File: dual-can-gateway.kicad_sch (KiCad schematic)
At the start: 82 parts, among them J3 Conn_01x02_Pin, Q1 AO3401A, Q2 2N7002, U1 STM32F446RETx, U2 STM32F446RETx, U3 ESP32-WROOM-32UE, U4 TJA1044GT-3, U5 TJA1044GT-3, U6 TJA1055T, U7 TJA1055T, U8 LM2596S-5, U9 AMS1117-3.3

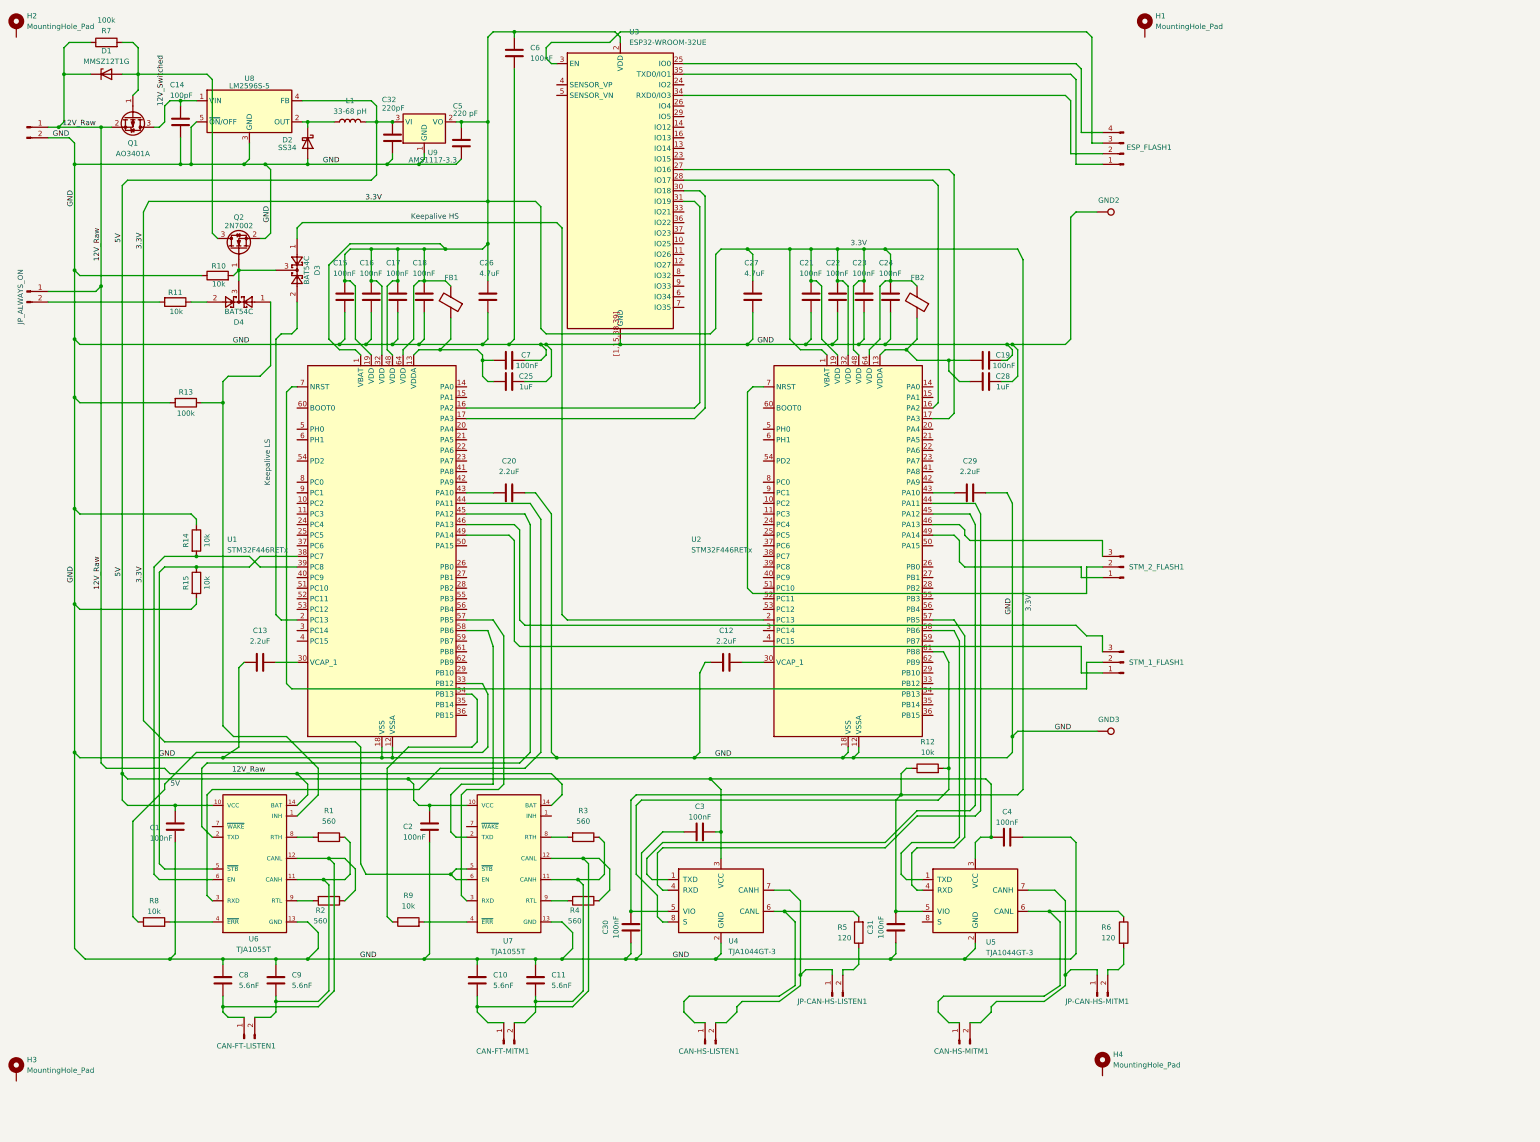
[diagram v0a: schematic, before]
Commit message: proper caps added
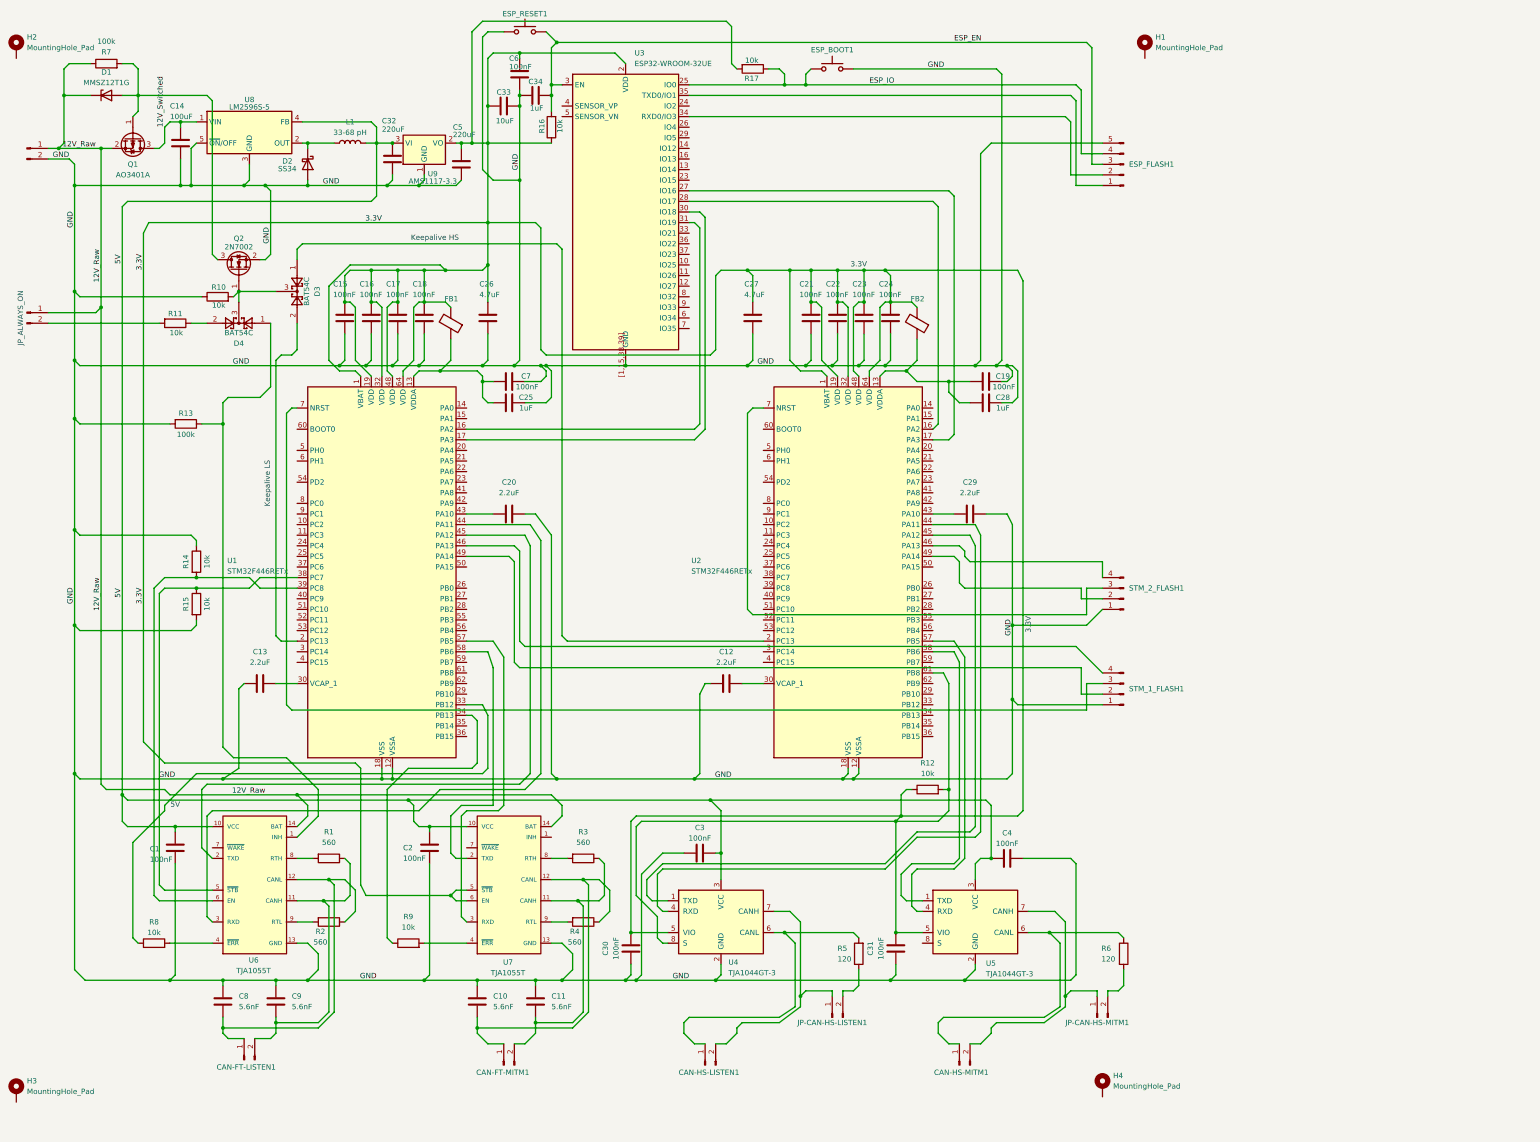
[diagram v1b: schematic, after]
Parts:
- removed ESP_FLASH1: Conn_01x04_Pin, Connector_PinHeader_2.54mm:PinHeader_1x04_P2.54mm_Vertical, symbol Connector:Conn_01x04_Pin
- removed GND2, GND3: TestPoint, Connector_PinHeader_2.54mm:PinHeader_1x01_P2.54mm_Vertical, symbol Connector:TestPoint
- removed STM_1_FLASH1, STM_2_FLASH1: Conn_01x03_Pin, Connector_PinHeader_2.54mm:PinHeader_1x03_P2.54mm_Vertical, symbol Connector:Conn_01x03_Pin
- added C33: 10uF, Capacitor_SMD:C_0805_2012Metric, symbol Device:C
- added C34: 1uF, Capacitor_SMD:C_0805_2012Metric, symbol Device:C
- added ESP_BOOT1: ESP_BOOT, Button_Switch_SMD:SW_Tactile_SPST_NO_Straight_CK_PTS636Sx25SMTRLFS, symbol Switch:SW_Push
- added ESP_FLASH1: Conn_01x05_Pin, Connector_PinHeader_2.54mm:PinHeader_1x05_P2.54mm_Vertical, symbol Connector:Conn_01x05_Pin
- added ESP_RESET1: ESP_RESET, Button_Switch_SMD:SW_Tactile_SPST_NO_Straight_CK_PTS636Sx25SMTRLFS, symbol Switch:SW_Push
- added R16, R17: 10k, Resistor_SMD:R_0805_2012Metric, symbol Device:R
- added STM_1_FLASH1, STM_2_FLASH1: Conn_01x04_Pin, Connector_PinHeader_2.54mm:PinHeader_1x04_P2.54mm_Vertical, symbol Connector:Conn_01x04_Pin
- C14: value 100pF -> 100uF; footprint Capacitor_SMD:C_0805_2012Metric -> Capacitor_Tantalum_SMD:CP_EIA-7343-40_Kemet-Y_HandSolder
- C32: value 220pF -> 220uF; footprint Capacitor_SMD:C_0805_2012Metric -> Capacitor_Tantalum_SMD:CP_EIA-6032-28_Kemet-C_HandSolder
- C5: value 220 pF -> 220uF; footprint Capacitor_SMD:C_0805_2012Metric -> Capacitor_Tantalum_SMD:CP_EIA-6032-28_Kemet-C_HandSolder
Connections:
- net 3.3V: now also R12.2, U2.61 (PB8), U4.8 (S), C33.1, R16.1, R17.2
- net GND: now also C33.2, C34.2, ESP_BOOT1.2, ESP_FLASH1.5 (Pin_5), ESP_RESET1.1, STM_1_FLASH1.1 (Pin_1), STM_2_FLASH1.1 (Pin_1)
- net at U3.35 (TXD0/IO1): now also ESP_FLASH1.1 (Pin_1)
- net at U3.34 (RXD0/IO3): now also ESP_FLASH1.2 (Pin_2)
- net ESP_EN: now reaches U3.3 (EN)
- net ESP_EN: now also C34.1, ESP_FLASH1.3 (Pin_3), ESP_RESET1.2, R16.2
- net ESP_IO: now reaches U3.25 (IO0)
- net ESP_IO: now also ESP_BOOT1.1, ESP_FLASH1.4 (Pin_4), R17.1
- net at U2.46 (PA13): now also STM_2_FLASH1.4 (Pin_4)
- net at U2.49 (PA14): now also STM_2_FLASH1.2 (Pin_2)
- net at U2.7 (NRST): now also STM_2_FLASH1.3 (Pin_3)
- net at U1.49 (PA14): now also STM_1_FLASH1.2 (Pin_2)
- net at U1.7 (NRST): now also STM_1_FLASH1.3 (Pin_3)
- net at U1.46 (PA13): now also STM_1_FLASH1.4 (Pin_4)
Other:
- moved on the sheet: C1, C10, C11, C12, C13, C14, C15, C16, C17, C18, C19, C2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

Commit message: we're getting there
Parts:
- removed STM_1_FLASH1, STM_2_FLASH1: Conn_01x04_Pin, Connector_PinHeader_2.54mm:PinHeader_1x04_P2.54mm_Vertical, symbol Connector:Conn_01x04_Pin
- removed U1, U2: STM32F446RETx, Package_QFP:LQFP-64_10x10mm_P0.5mm, symbol MCU_ST_STM32F4:STM32F446RETx
- added C35, C36: 100nf, Capacitor_SMD:C_0805_2012Metric, symbol Device:C
- added R18: 10k, Resistor_SMD:R_0805_2012Metric, symbol Device:R
- added STM_FLASH1, STM_FLASH2: Conn_01x05_Pin, Connector_PinHeader_2.54mm:PinHeader_1x05_P2.54mm_Vertical, symbol Connector:Conn_01x05_Pin
- added U1, U2: STM32F405RGTx, Package_QFP:LQFP-64_10x10mm_P0.5mm, symbol MCU_ST_STM32F4:STM32F405RGTx
- L1: value 33-68 pH -> 33-68 uH
- U6, U7: value TJA1055T -> TJA1055T/3
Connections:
- net 3.3V: now also STM_FLASH1.1 (Pin_1), STM_FLASH2.1 (Pin_1), U1.1 (VBAT), U1.19 (VDD), U1.32 (VDD), U1.48 (VDD), U1.64 (VDD), U2.1 (VBAT), U2.19 (VDD), U2.32 (VDD), U2.48 (VDD), U2.64 (VDD); no longer R12.1, R12.2, U4.8 (S)
- net GND: now also C20.1, C29.1, H1.1, H3.1, H4.1, R12.1, U4.8 (S), U5.8 (S), C35.1, C36.2, R18.1, STM_FLASH1.2 (Pin_2), STM_FLASH2.2 (Pin_2), U1.12 (VSSA), U1.18 (VSS), U1.63 (VSS), U2.12 (VSSA), U2.18 (VSS), U2.63 (VSS); no longer C20.2, C29.2
- net at R9.1: now also U1.33 (PB12)
- net at U4.1 (TXD): now also U2.45 (PA12)
- net at U4.4 (RXD): now also U2.44 (PA11)
- net at C13.2: now also U1.31 (VCAP_1)
- net at D3.1: now also U2.2 (PC13)
- net at D3.2: now also U1.2 (PC13)
- net at R14.2, U6.6 (EN): now also U1.39 (PC8)
- net at C19.1, C28.1, FB2.1: now also U2.13 (VDDA)
- net at U3.28 (IO17): now also U2.16 (PA2)
- net at U3.27 (IO16): now also U2.17 (PA3)
- net at C12.2: now also U2.31 (VCAP_1)
- net at U5.4 (RXD): now also U2.57 (PB5)
- net at U5.1 (TXD): now also U2.58 (PB6)
- net at C25.1, C7.1, FB1.1: now also U1.13 (VDDA)
- net at U6.2 (TXD): now also U1.45 (PA12)
- net at U6.3 (RXD): now also U1.44 (PA11)
- net at R15.1, U6.5 (~{STB}): now also U1.38 (PC7)
- net at U7.2 (TXD): now also U1.58 (PB6)
- net at U7.3 (RXD): now also U1.57 (PB5)
- net at U3.30 (IO18): now also U1.17 (PA3)
- net at U3.31 (IO19): now also U1.16 (PA2)
- net at R8.1: now also U1.30 (PB11)
- new net: STM_FLASH1.3 (Pin_3), U1.49 (PA14)
- new net: C36.1, STM_FLASH1.4 (Pin_4), U1.7 (NRST)
- new net: STM_FLASH1.5 (Pin_5), U1.46 (PA13)
- new net: R12.2, U2.60 (BOOT0)
- new net: C29.2, U2.47 (VCAP_2)
- new net: C35.2, STM_FLASH2.4 (Pin_4), U2.7 (NRST)
- new net: R18.2, U1.60 (BOOT0)
- new net: C20.2, U1.47 (VCAP_2)
- new net: STM_FLASH2.5 (Pin_5), U2.46 (PA13)
- new net: STM_FLASH2.3 (Pin_3), U2.49 (PA14)
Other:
- note removed: "3.3V"
- moved on the sheet: C1, C10, C11, C12, C13, C2, C20, C29, C3, C30, C31, C4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

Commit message: v1.1 almost done, new preview
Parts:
- added C37: 100nF, Capacitor_SMD:C_0805_2012Metric, symbol Device:C
- added D5: SMCJ24CA, Diode_SMD:D_SMC, symbol Device:D_TVS
- added R19: 10k, Resistor_SMD:R_0805_2012Metric, symbol Device:R
- C14: footprint Capacitor_Tantalum_SMD:CP_EIA-7343-40_Kemet-Y_HandSolder -> Capacitor_SMD:CP_Elec_6.3x7.7
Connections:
- net 12V_Switched: now also C37.2
- net GND: now also C37.1, D5.1 (A1)
- net at D1.2 (A), Q2.3 (D), R7.2: now also R19.1; no longer Q1.1 (G)
- net 12V_Raw renamed 12V_Protected
- net 12V_Protected: now also D5.2 (A2)
- new net: Q1.1 (G), R19.2
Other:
- moved on the sheet: C14, D1, R7

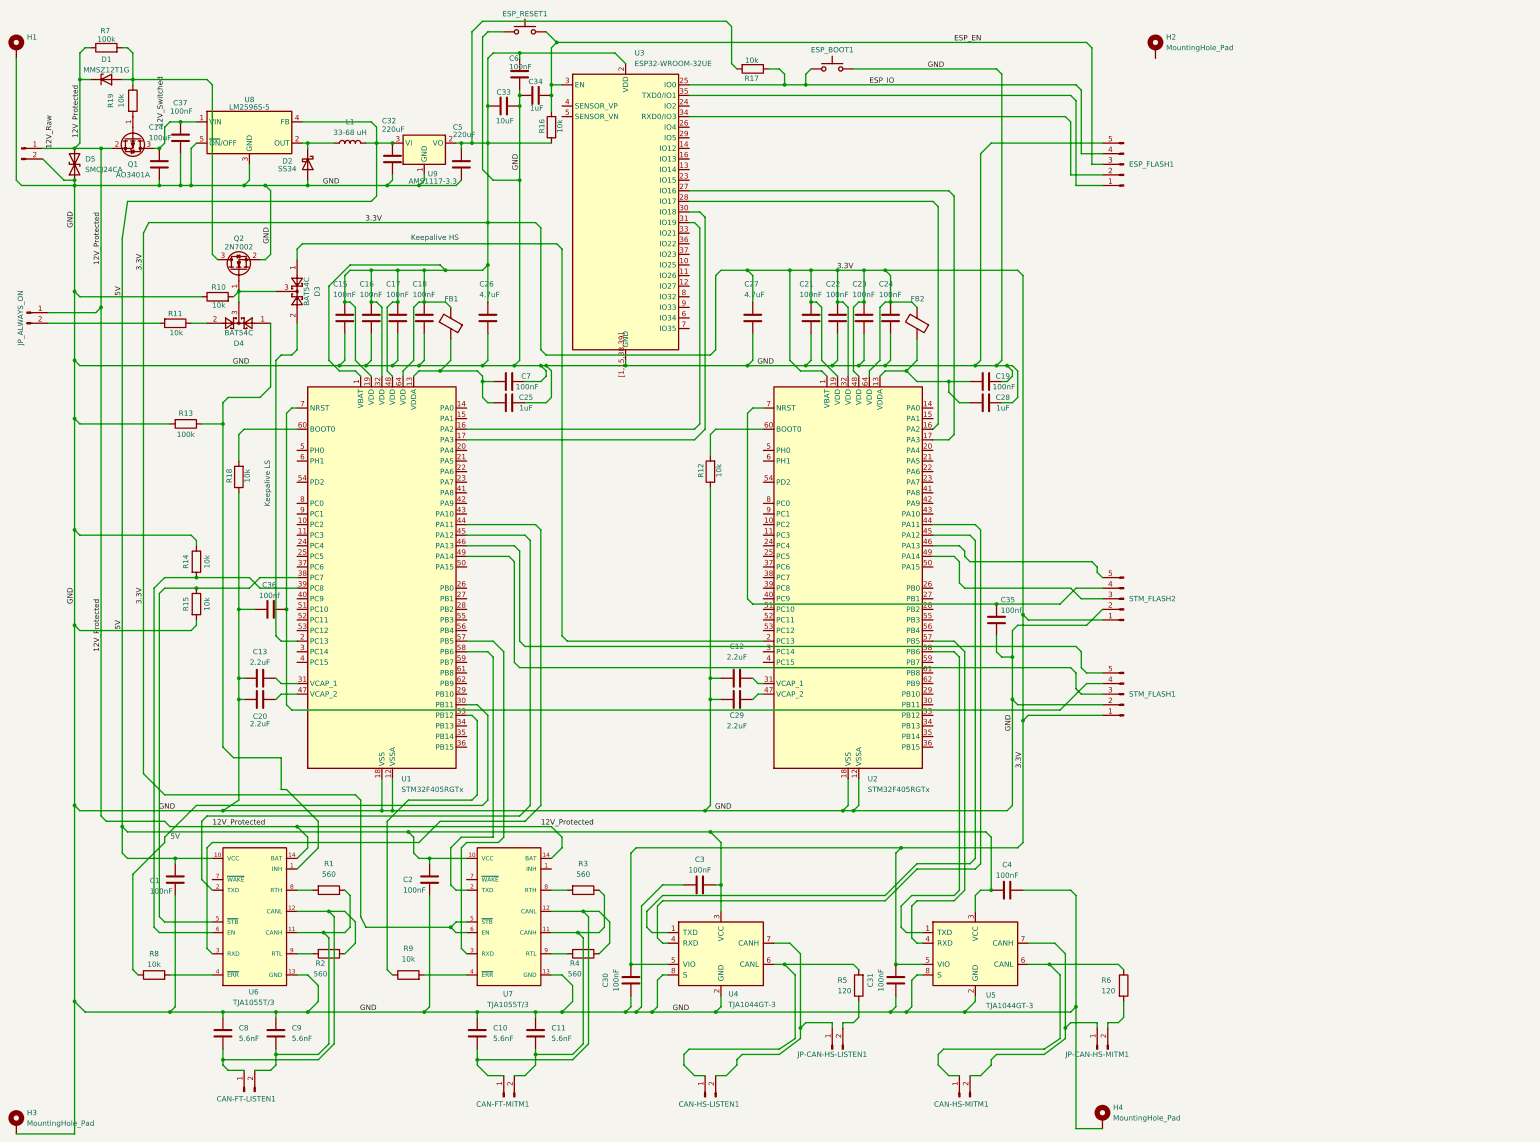
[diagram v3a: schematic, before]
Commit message: added inter mcu communication as well as debug led
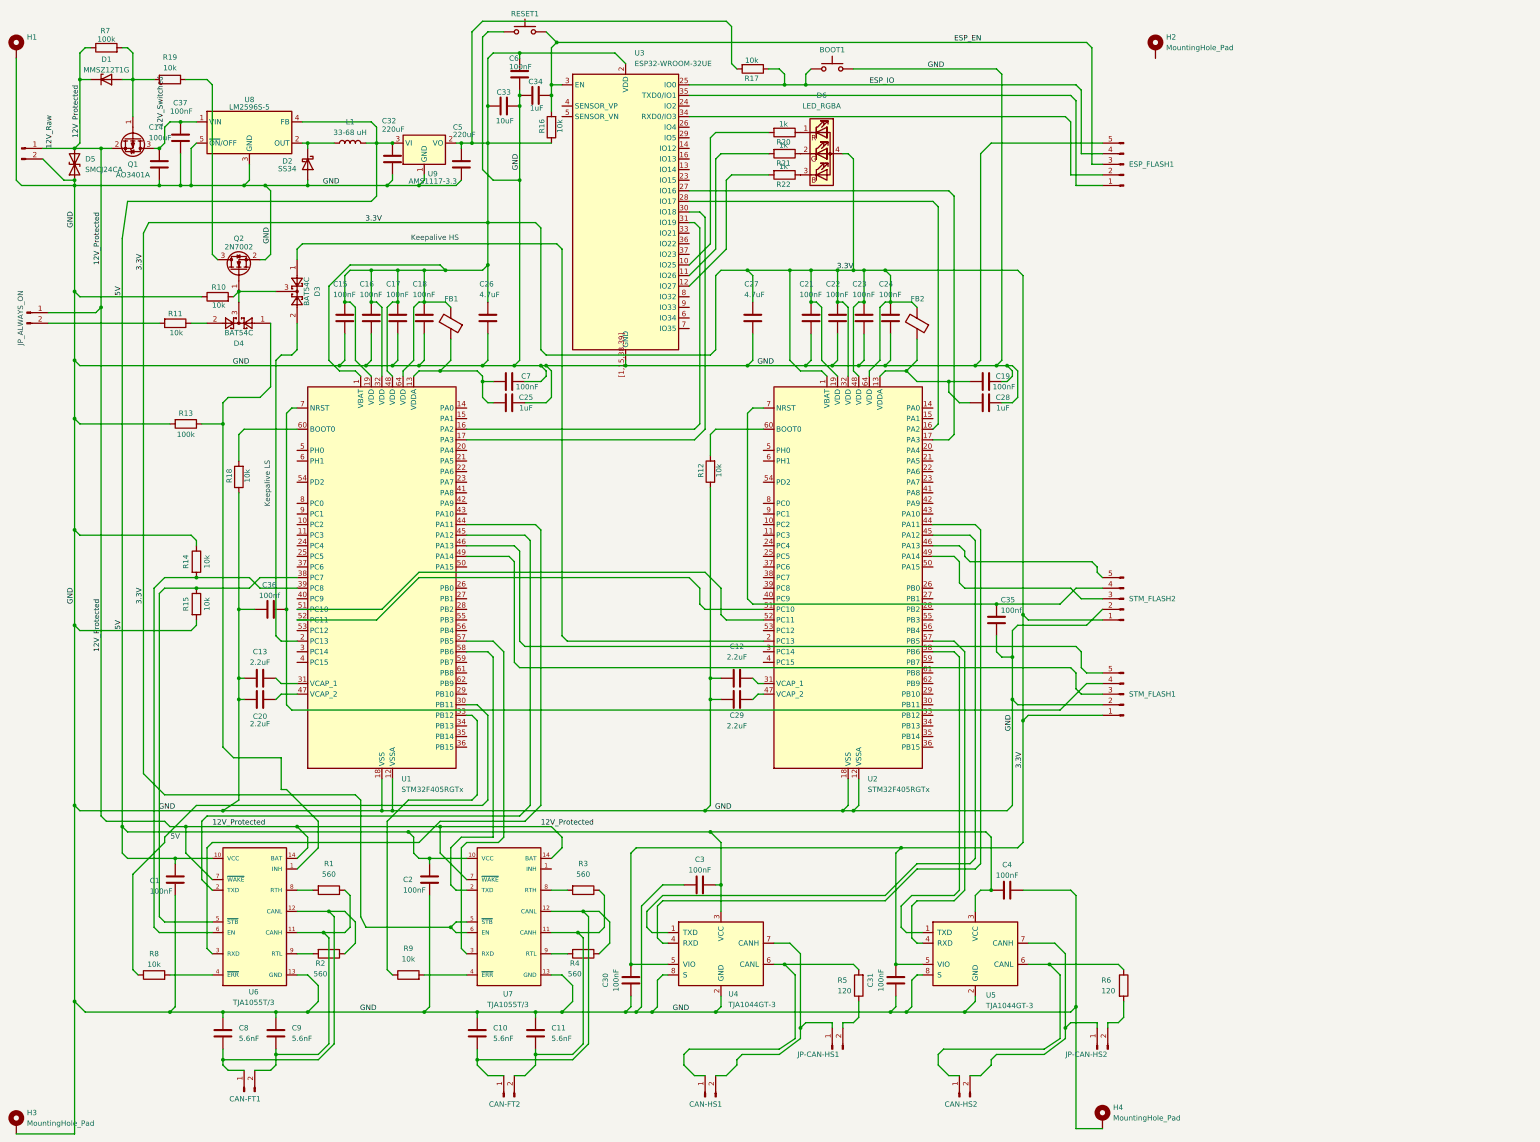
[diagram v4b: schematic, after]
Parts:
- added D6: LED_RGBA, LED_SMD:LED_RGB_1210, symbol Device:LED_RGBA
- added R20, R21, R22: 1k, Resistor_SMD:R_0805_2012Metric, symbol Device:R
- renumbered ESP_BOOT1 to BOOT1, CAN-FT-LISTEN1 to CAN-FT1, CAN-FT-MITM1 to CAN-FT2, CAN-HS-LISTEN1 to CAN-HS1, CAN-HS-MITM1 to CAN-HS2, JP-CAN-HS-LISTEN1 to JP-CAN-HS1, JP-CAN-HS-MITM1 to JP-CAN-HS2, ESP_RESET1 to RESET1
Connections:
- net 12V_Protected: now also U6.7 (~{WAKE}), U7.7 (~{WAKE})
- net 3.3V: now also D6.4 (A)
- net at Q2.3 (D), R19.1: no longer D1.2 (A), R7.2
- net at Q1.1 (G), R19.2: now also D1.2 (A), R7.2
- net at U1.51 (PC10): now also U2.52 (PC11)
- net at U1.52 (PC11): now also U2.51 (PC10)
- net at U3.10 (IO25): now also R20.2
- net at U3.11 (IO26): now also R21.2
- net at U3.12 (IO27): now also R22.2
- new net: D6.1 (RK), R20.1
- new net: D6.3 (BK), R22.1
- new net: D6.2 (GK), R21.1
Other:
- moved on the sheet: R19
